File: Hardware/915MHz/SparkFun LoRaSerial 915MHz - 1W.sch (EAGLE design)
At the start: 96 parts, among them J1 QWIIC_RIGHT_ANGLE, J3 USB C, J4 JTAG, Q1 20V/0.2A/8MHz/1.2Ω/1Vth, Q2 20V/0.2A/8MHz/1.2Ω/1Vth, Q3 600mA/40V, Q4 600mA/40V, Q5 600mA/40V, Q6 600mA/40V, Q8 20V/4.2A/52mΩ/1.4W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

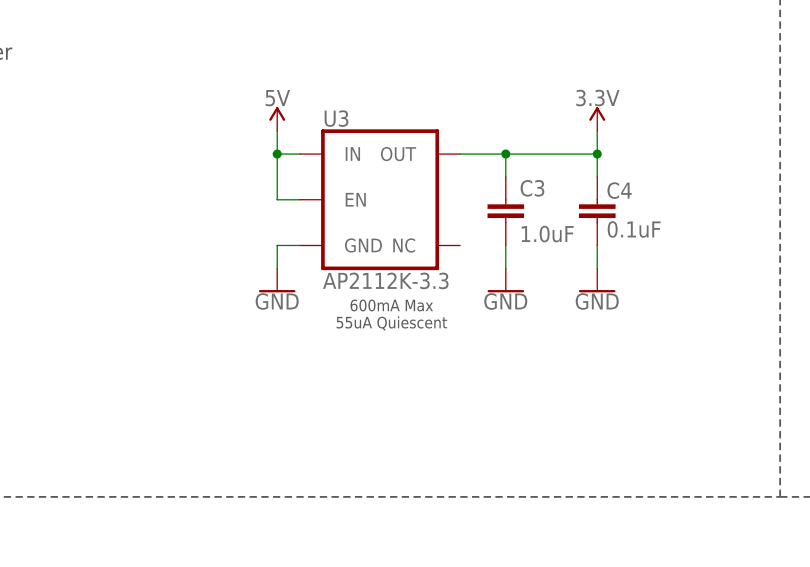
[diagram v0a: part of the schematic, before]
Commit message: Change to in stock 3.3V regulator
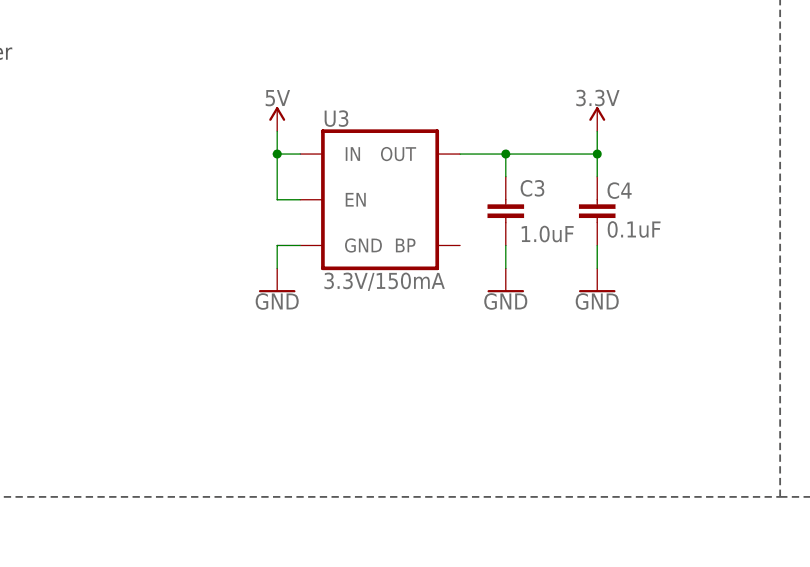
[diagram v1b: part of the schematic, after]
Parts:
- U3: value AP2112K-3.3 -> 3.3V/150mA; device SparkFun-IC-Power:V_REG_AP2112K-3.3V -> SparkFun-IC-Power:V_REG_MIC52053.3V
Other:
- note removed: "600mA Max 55uA Quiescent"
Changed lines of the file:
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@@
 <part name="C3" library="SparkFun-Capacitors" deviceset="1.0UF" device="-0603-16V-10%-X7R" value="1.0uF"/>
 <part name="C4" library="SparkFun-Capacitors" deviceset="0.1UF" device="-0603-25V-5%" value="0.1uF"/>
-<part name="U3" library="SparkFun-IC-Power" deviceset="V_REG_AP2112" device="K-3.3V" value="AP2112K-3.3"/>
+<part name="U3" library="SparkFun-IC-Power" deviceset="V_REG_MIC5205" device="3.3V" value="3.3V/150mA"/>
 <part name="SUPPLY38" library="SparkFun-PowerSymbols" deviceset="3.3V" device=""/>
 <part name="GND53" library="SparkFun-PowerSymbols" deviceset="GND" device=""/>
@@
 <text x="172.974" y="40.386" size="2.54" layer="94" font="vector" align="center">Cable Port</text>
 <text x="251.46" y="137.16" size="2.54" layer="94" font="vector" rot="MR180" align="center">Voltage Regulation</text>
-<text x="248.92" y="96.52" size="1.27" layer="97" font="vector" align="center">600mA Max
-55uA Quiescent</text>
 <wire x1="88.9" y1="149.86" x2="0" y2="149.86" width="0.2032" layer="97" style="longdash"/>
 <wire x1="147.32" y1="76.2" x2="292.1" y2="76.2" width="0.2032" layer="97" style="longdash"/>
@@
 <attribute name="VALUE" x="272.796" y="105.029" size="1.778" layer="96" font="vector"/>
 </instance>
-<instance part="U3" gate="G$1" x="248.92" y="109.22" smashed="yes">
+<instance part="U3" gate="U1" x="248.92" y="109.22" smashed="yes">
 <attribute name="NAME" x="241.3" y="117.348" size="1.778" layer="95" font="vector"/>
 <attribute name="VALUE" x="241.3" y="101.092" size="1.778" layer="96" font="vector" align="top-left"/>
@@
 <wire x1="238.76" y1="104.14" x2="236.22" y2="104.14" width="0.1524" layer="91"/>
 <wire x1="236.22" y1="104.14" x2="236.22" y2="101.6" width="0.1524" layer="91"/>
-<pinref part="U3" gate="G$1" pin="GND"/>
+<pinref part="U3" gate="U1" pin="GND"/>
 <pinref part="GND53" gate="1" pin="GND"/>
 </segment>
@@
 <wire x1="271.78" y1="111.76" x2="271.78" y2="114.3" width="0.1524" layer="91"/>
 <junction x="261.62" y="114.3"/>
-<pinref part="U3" gate="G$1" pin="OUT"/>
+<pinref part="U3" gate="U1" pin="OUT"/>
 <pinref part="C3" gate="G$1" pin="1"/>
 <pinref part="C4" gate="G$1" pin="2"/>
@@
 </segment>
 <segment>
-<pinref part="U3" gate="G$1" pin="IN"/>
+<pinref part="U3" gate="U1" pin="IN"/>
 <wire x1="238.76" y1="114.3" x2="236.22" y2="114.3" width="0.1524" layer="91"/>
 <wire x1="236.22" y1="116.84" x2="236.22" y2="114.3" width="0.1524" layer="91"/>
 <pinref part="SUPPLY11" gate="G$1" pin="5V"/>
-<pinref part="U3" gate="G$1" pin="EN"/>
+<pinref part="U3" gate="U1" pin="EN"/>
 <wire x1="238.76" y1="109.22" x2="236.22" y2="109.22" width="0.1524" layer="91"/>
 <wire x1="236.22" y1="109.22" x2="236.22" y2="114.3" width="0.1524" layer="91"/>

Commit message: Change RSSI LED resistors to 22 ohm
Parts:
- R20, R21, R22, R9: value 220 -> 22Ω; device SparkFun-Resistors:220OHM-0603-1/10W-1% -> SparkFun-Resistors:22OHM-0603-1/10W-1%
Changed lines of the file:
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@@
 <part name="D5" library="SparkFun-LED" deviceset="LED-RED" device="0603" value="RED"/>
 <part name="R1" library="SparkFun-Resistors" deviceset="1KOHM" device="-0603-1/10W-1%" value="1k"/>
-<part name="R9" library="SparkFun-Resistors" deviceset="220OHM" device="-0603-1/10W-1%" value="220"/>
+<part name="R9" library="SparkFun-Resistors" deviceset="22OHM" device="-0603-1/10W-1%" value="22Ω"/>
 <part name="GND10" library="SparkFun-PowerSymbols" deviceset="GND" device=""/>
 <part name="GND16" library="SparkFun-PowerSymbols" deviceset="GND" device=""/>
@@
 <part name="SUPPLY10" library="SparkFun-PowerSymbols" deviceset="5V" device=""/>
 <part name="SUPPLY14" library="SparkFun-PowerSymbols" deviceset="5V" device=""/>
-<part name="R20" library="SparkFun-Resistors" deviceset="220OHM" device="-0603-1/10W-1%" value="220"/>
+<part name="R20" library="SparkFun-Resistors" deviceset="22OHM" device="-0603-1/10W-1%" value="22Ω"/>
 <part name="D1" library="SparkFun-LED" deviceset="LED-GREEN" device="0603" value="GREEN"/>
 <part name="GND14" library="SparkFun-PowerSymbols" deviceset="GND" device=""/>
-<part name="R21" library="SparkFun-Resistors" deviceset="220OHM" device="-0603-1/10W-1%" value="220"/>
+<part name="R21" library="SparkFun-Resistors" deviceset="22OHM" device="-0603-1/10W-1%" value="22Ω"/>
 <part name="D7" library="SparkFun-LED" deviceset="LED-GREEN" device="0603" value="GREEN"/>
 <part name="GND15" library="SparkFun-PowerSymbols" deviceset="GND" device=""/>
 <part name="D8" library="SparkFun-LED" deviceset="LED-GREEN" device="0603" value="GREEN"/>
-<part name="R22" library="SparkFun-Resistors" deviceset="220OHM" device="-0603-1/10W-1%" value="220"/>
+<part name="R22" library="SparkFun-Resistors" deviceset="22OHM" device="-0603-1/10W-1%" value="22Ω"/>
 <part name="GND26" library="SparkFun-PowerSymbols" deviceset="GND" device=""/>
 <part name="SUPPLY18" library="SparkFun-PowerSymbols" deviceset="3.3V" device=""/>

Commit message: Add 433MHz and 868MHz designs
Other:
- note added: "433MHz: 10/20"
- note added: "868MHz: 3.3/10"
- note added: "915MHz: 10/10"
- note added: "IDs:"
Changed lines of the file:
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@@
 <wire x1="88.9" y1="76.2" x2="88.9" y2="149.86" width="0.2032" layer="97" style="longdash"/>
 <wire x1="66.04" y1="0" x2="66.04" y2="76.2" width="0.2032" layer="97" style="longdash"/>
+<text x="7.62" y="134.62" size="1.778" layer="97" align="center-left">IDs:</text>
+<text x="7.62" y="132.08" size="1.778" layer="97" align="center-left">915MHz: 10/10</text>
+<text x="7.62" y="129.54" size="1.778" layer="97" align="center-left">868MHz: 3.3/10</text>
+<text x="7.62" y="127" size="1.778" layer="97" align="center-left">433MHz: 10/20</text>
 </plain>
 <instances>

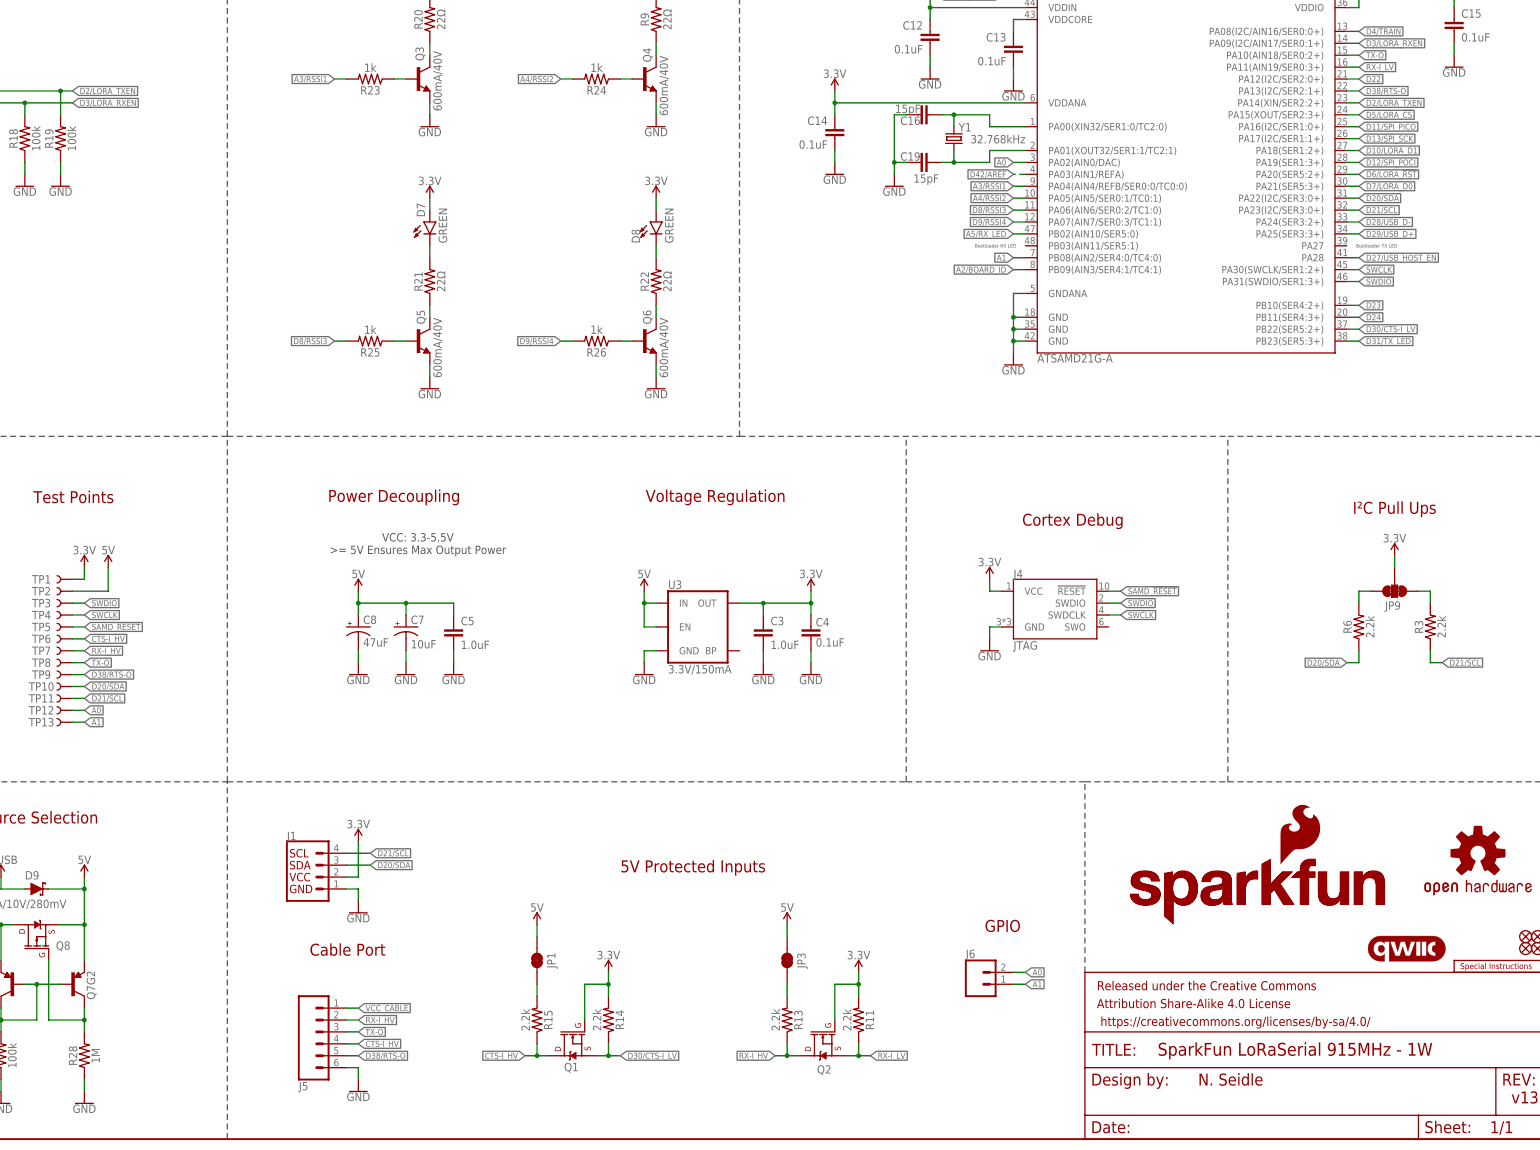
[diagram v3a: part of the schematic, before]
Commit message: Update schematics with flow control notes
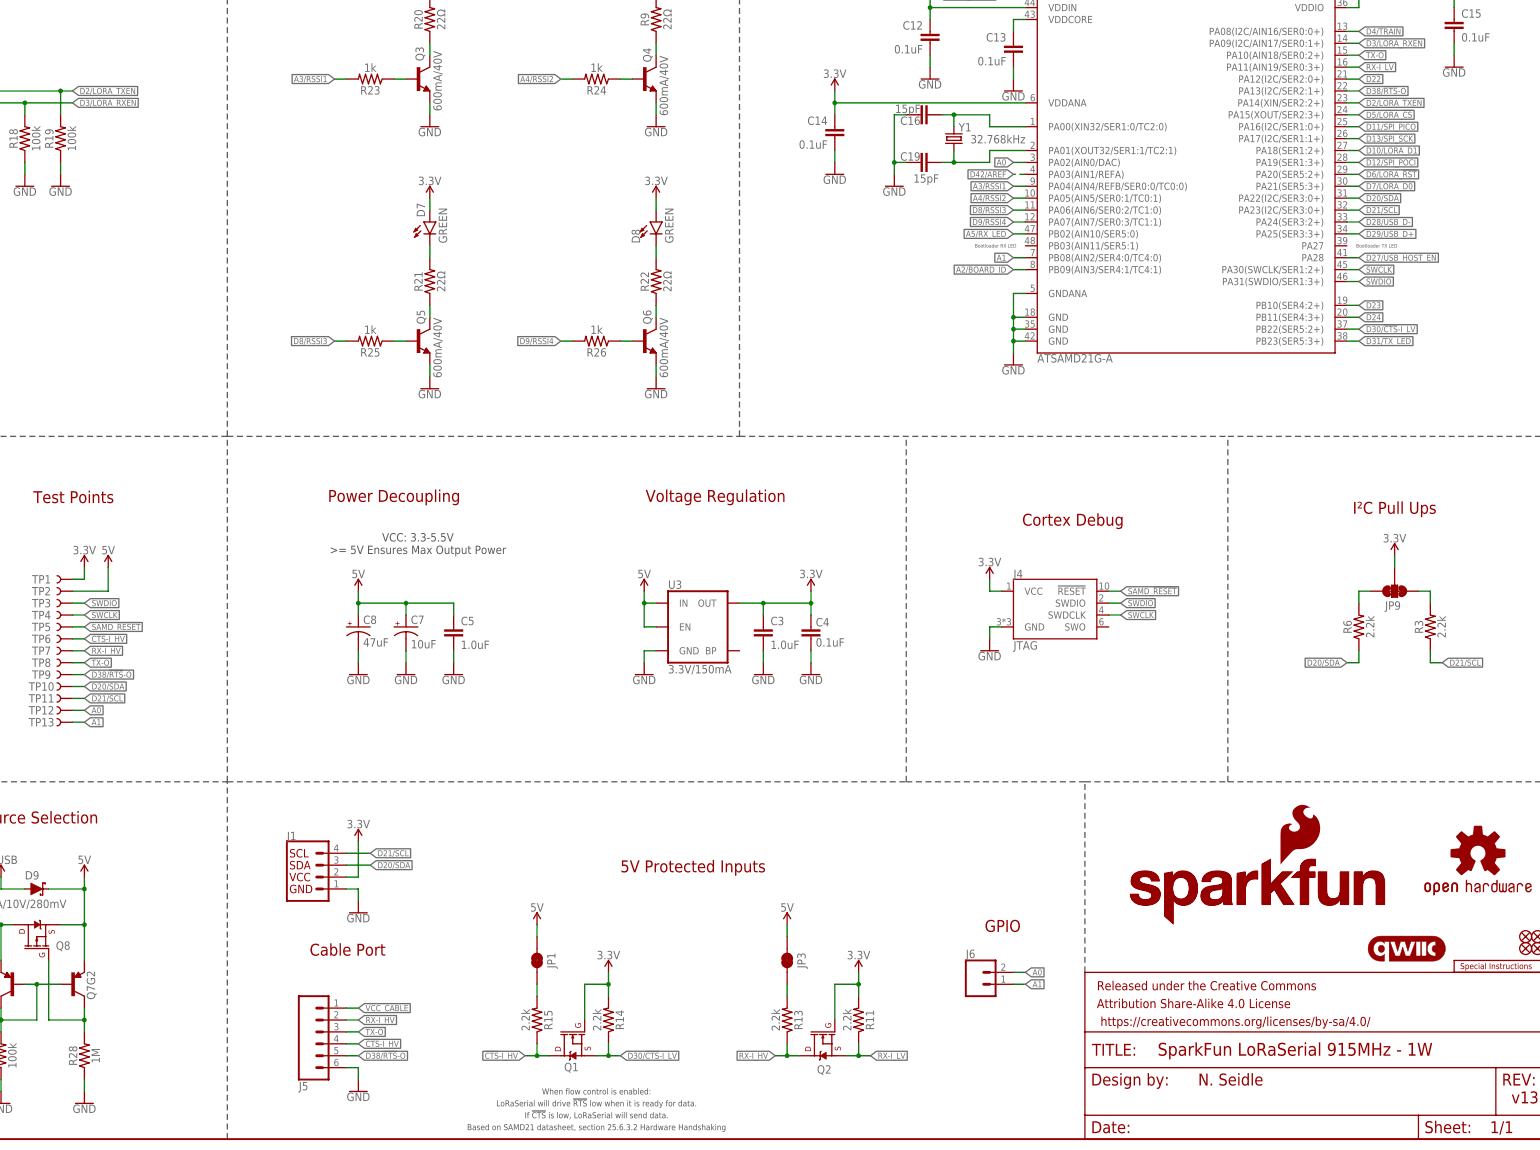
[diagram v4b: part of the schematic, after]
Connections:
- net CTS-I_HV renamed !CTS!-I_HV
- net D30/CTS-I_LV renamed D30/!CTS!-I_LV
- net D38/RTS-O renamed D38/!RTS!-O
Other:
- note added: "Based on SAMD21 datasheet, section 25.6.3.2 Hardware Handshaking"
- note added: "If !CTS! is low, LoRaSerial will send data."
- note added: "LoRaSerial will drive !RTS! low when it is ready for data."
- note added: "When flow control is enabled:"
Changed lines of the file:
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@@
 <text x="7.62" y="129.54" size="1.778" layer="97" align="center-left">868MHz: 3.3/10</text>
 <text x="7.62" y="127" size="1.778" layer="97" align="center-left">433MHz: 10/20</text>
+<text x="226.06" y="7.62" size="1.27" layer="97" font="vector" align="center">LoRaSerial will drive !RTS! low when it is ready for data.</text>
+<text x="226.06" y="5.08" size="1.27" layer="97" font="vector" align="center">If !CTS! is low, LoRaSerial will send data.</text>
+<text x="226.06" y="2.54" size="1.27" layer="97" font="vector" align="center">Based on SAMD21 datasheet, section 25.6.3.2 Hardware Handshaking</text>
+<text x="226.06" y="10.16" size="1.27" layer="97" font="vector" align="center">When flow control is enabled:</text>
 </plain>
 <instances>
@@
 </segment>
 </net>
-<net name="D30/CTS-I_LV" class="0">
+<net name="D30/!CTS!-I_LV" class="0">
 <segment>
 <pinref part="U2" gate="G$1" pin="PB22(SER5:2+)"/>
@@
 </segment>
 </net>
-<net name="D38/RTS-O" class="0">
+<net name="D38/!RTS!-O" class="0">
 <segment>
 <pinref part="U2" gate="G$1" pin="PA13(I2C/SER2:1+)"/>
@@
 </segment>
 </net>
-<net name="CTS-I_HV" class="0">
+<net name="!CTS!-I_HV" class="0">
 <segment>
 <label x="175.26" y="20.32" size="1.27" layer="95" font="vector" xref="yes"/>
